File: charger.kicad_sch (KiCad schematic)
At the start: 14 parts, among them J5 USB_C_Receptacle_USB2.0_16P, Q1 BSS84, Q2 BSS670S2, U16 USBLC6-2SC6, U3 MIC5205-3.3YM5, U4 MCP73833-xxx-UN

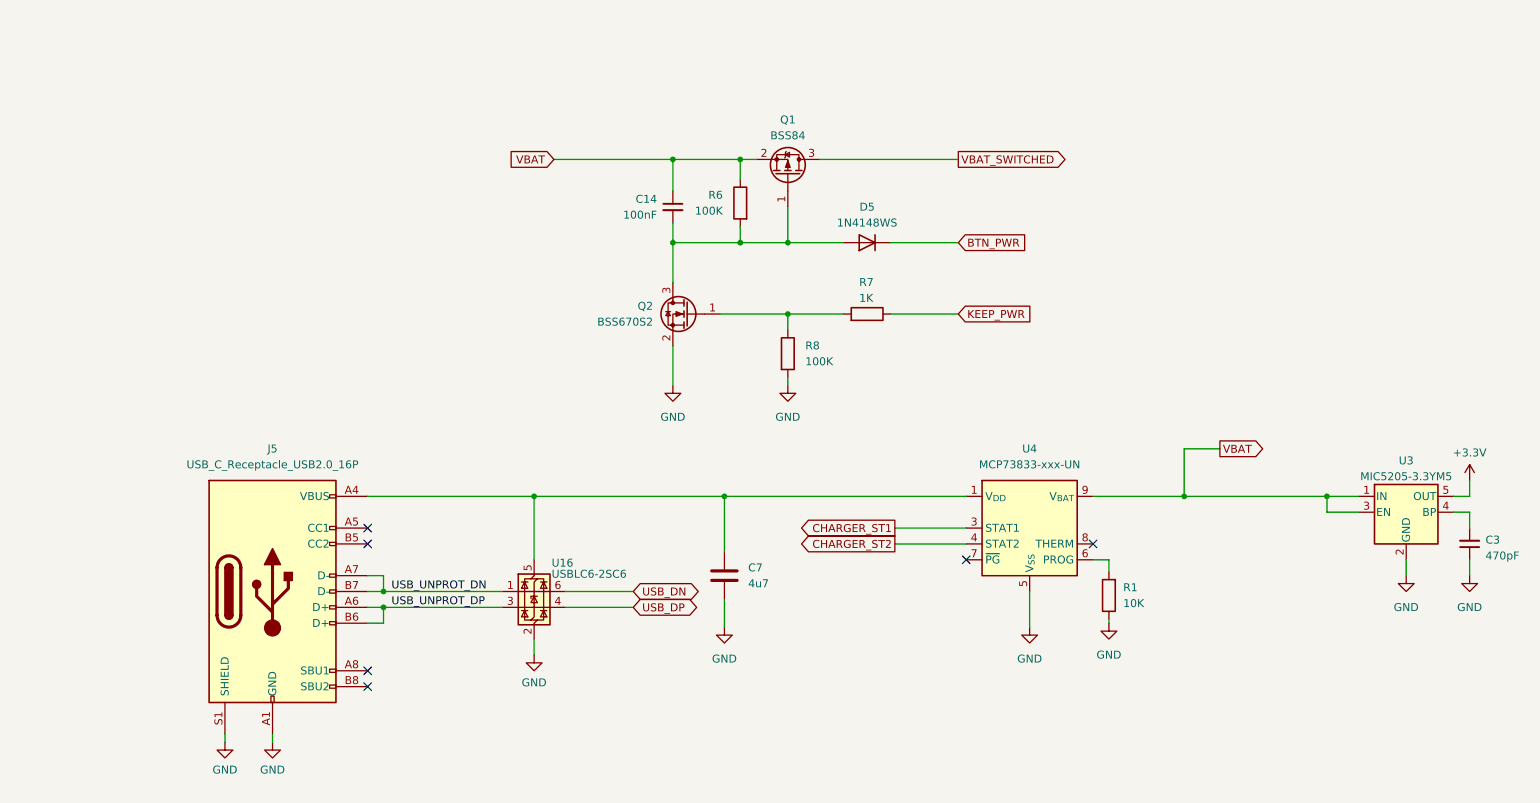
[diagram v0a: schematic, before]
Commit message: Board had been routedy
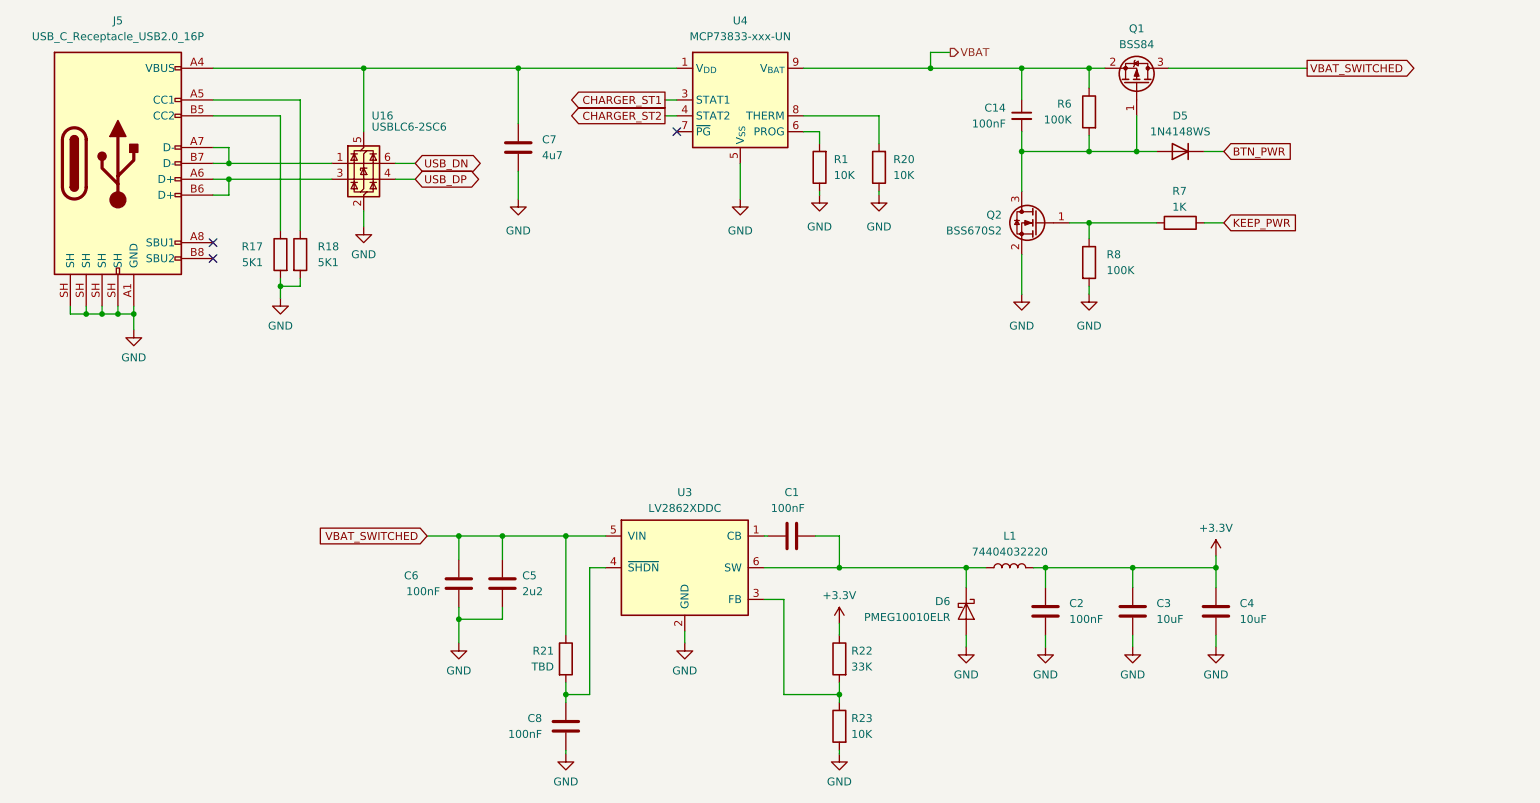
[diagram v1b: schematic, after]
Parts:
- removed C3: 470pF, Capacitor_SMD:C_0603_1608Metric, symbol Device:C_Small
- removed U3: MIC5205-3.3YM5, Package_TO_SOT_SMD:SOT-23-5, symbol Regulator_Linear:MIC5205-3.3YM5
- added C1, C2, C6, C8: 100nF, Capacitor_SMD:C_0603_1608Metric, symbol Device:C
- added C3: 10uF, Capacitor_SMD:C_0603_1608Metric, symbol Device:C
- added C4: 10uF, Capacitor_SMD:C_0805_2012Metric, symbol Device:C
- added C5: 2u2, Capacitor_SMD:C_0805_2012Metric, symbol Device:C
- added D6: PMEG10010ELR, Diode_SMD:Nexperia_CFP3_SOD-123W, symbol Diode:PMEG10010ELR
- added L1: 74404032220, Inductor_SMD:L_Wuerth_MAPI-3015, symbol Device:L
- added R17, R18: 5K1, Resistor_SMD:R_0603_1608Metric, symbol Device:R
- added R20, R23: 10K, Resistor_SMD:R_0603_1608Metric, symbol Device:R
- added R21: TBD, Resistor_SMD:R_0603_1608Metric, symbol Device:R
- added R22: 33K, Resistor_SMD:R_0603_1608Metric, symbol Device:R
- added U3: LV2862XDDC, Package_TO_SOT_SMD:SOT-23-6, symbol Regulator_Switching:LV2862XDDC
- R1: footprint Resistor_SMD:R_0402_1005Metric -> Resistor_SMD:R_0603_1608Metric
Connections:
- net +3.3V: now also C2.2, C3.2, C4.2, L1.2, R22.1
- net GND: now also J5.SH, C2.1, C3.1, C4.1, C5.1, C6.1, C8.1, D6.2 (A), R17.2, R18.2, R20.1, R23.2, U3.2 (GND); no longer J5.S1 (SHIELD)
- net VBAT_SWITCHED: now also C5.2, C6.2, R21.1, U3.5 (VIN)
- net at J5.A5 (CC1): now also R18.1
- net at J5.B5 (CC2): now also R17.1
- net at U4.8 (THERM): now also R20.2
- new net: C1.2, D6.1 (K), L1.1, U3.6 (SW)
- new net: C1.1, U3.1 (CB)
- new net: R22.2, R23.1, U3.3 (FB)
- new net: C8.2, R21.2, U3.4 (~{SHDN})
- no-connect marks 6 -> 3
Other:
- moved on the sheet: C14, C7, D5, Q1, Q2, R1, R6, R7, R8, U16, U4

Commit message: Daily save
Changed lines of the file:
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@@
 	(wire
 		(pts
-			(xy 94.615 106.045) (xy 99.695 106.045)
+			(xy 83.82 106.045) (xy 99.695 106.045)
 		)
 		(stroke
@@
 	(global_label "VBAT_SWITCHED"
 		(shape input)
-		(at 94.615 106.045 180)
+		(at 83.82 106.045 180)
 		(fields_autoplaced yes)
 		(effects
@@
 		)
 		(property "Intersheetrefs" "${INTERSHEET_REFS}"
-			(at 76.9946 106.045 0)
+			(at 66.1996 106.045 0)
 			(hide yes)
 			(show_name no)
@@
 		)
 	)
+	(group "charger"
+		(lib_id "martonmiklos:charger")
+		(members "01e84fd5-f747-4020-8fd6-b8dcc2b74338" "03a726e8-f3e8-403e-924a-5ef765c4f7fc"
+			"03f131bc-6628-429a-b0a5-e3f5afa171e4" "0b628756-8c00-452b-a3bd-ef999dcb8288"
+			"0b82a914-d713-4daf-9dc4-990cb81dc069" "15827e9a-85e8-4dd6-bc7d-e9f6ff24fd2d"
+			"15aa98e9-b72d-46e3-ab74-56cddecf5905" "173c6623-909e-4824-a967-7bd19a3c97d4"
+			"238347b0-2046-4f9f-bff6-a5b2ada0af1e" "247ee5cc-030c-499e-9d8b-42cf448516b7"
+			"2b1602a1-1bb2-4b2e-9c42-5471c2828bd8" "2b3f2cf4-1d8e-4fd8-8ea6-2a000066a748"
+			"2b5e59b9-4754-44b4-a9e3-1f4f43548eff" "376efd5a-dcb1-49ac-a426-d0f8d062c864"
+			"377687a4-20e1-429a-927b-2d6216137319" "3c8d662e-433a-4f96-8204-c6cd305cf2e5"
+			"3f5b5540-a644-4c20-b592-0d633b188111" "3fde2300-c87d-4f69-a114-242149a44162"
+			"41765163-874c-43af-afa4-44d000001fc7" "442cabfd-17f5-4520-9de1-67ccdf6128c3"
+			"4453b4e2-24bb-4e59-8092-f0588bce46a0" "488b77b0-993e-4126-9e9e-be032d7f7890"
+			"4947df85-bb2c-4b75-b2ea-5ab3492b03b4" "4990c6a4-f824-4d5c-8455-599c775c8ad1"
+			"4adec73d-67c0-4a8b-b247-3fe800ffe248" "4ed56fd3-6be7-4b9e-853e-a8b9b717d92c"
+			"50a1eb87-f90e-4274-8e3c-f7c2477b2a9d" "51d7c8de-3539-4ee9-9edc-b2976a9c465b"
+			"52450477-23f9-4c73-acf5-7c7c3b8b462e" "55b3fa5f-76c7-49db-8516-2348f296e36e"
+			"5655d3c4-d9a3-429c-92f8-097bd0b7afd1" "5a170b1c-98c5-4d4d-a57b-8be4ebf1ed0f"
+			"5cfed881-f50f-46e9-8914-ab80adff6d16" "613ccada-4610-40d0-8e92-0e1ed197e285"
+			"65766a60-7b75-44ee-a0a9-f5928501c4b7" "676ae03b-85a6-4a64-85ba-633ca9625658"
+			"6c652ae5-12ce-464d-8867-881209a80aeb" "76a2fdcf-4a87-499f-80a2-e44584066a7d"
+			"7904565b-1804-4336-889a-a4ce34178e21" "7eb14095-606c-4043-a32c-7274450ad052"
+			"82acc906-3b09-4950-8317-9efc5bac570c" "8715af0d-f789-451c-887d-52f29fb580c9"
+			"8aa6c538-0075-4573-b337-a18bd0b0a999" "8f2a7e35-5af3-447e-a823-93f6e491f942"
+			"91127fee-99b5-4e89-91a1-d7f753c85a87" "92a9fef8-3b15-4087-a0ad-d5eff69b5456"
+			"954f9562-1f7b-4ee5-839e-3407e6830d32" "9a4b5429-6889-4350-84d7-955d2c48a51b"
+			"9e49f6a7-135d-4d5b-bfb8-e23c5b1003ae" "9e6087be-e4e2-4034-85cd-a9c03fec03cc"
+			"9e69fab5-6437-419a-b22c-62ba6257170f" "a329b400-aeb3-44c2-894a-a76a0c8a55cc"
+			"a55610d4-96c6-4b30-b669-a3477d539bc6" "af45645e-0808-4134-aa6b-30d80b51711b"
+			"b4252efc-8d8f-42ec-9a0a-9338a0eb963f" "b930e5d8-374a-45dd-ae95-636f2f37bd8c"
+			"ba6ce36a-0c0c-4108-9d7d-7e64598c8630" "c07f3d91-b843-4dbd-99e1-fca94b3a66ca"
+			"c0a90cf4-4a55-4374-a9bf-3989e4863e6c" "c6b61dfb-ee0a-4562-a8b9-56d9b76ccede"
+			"c8e050ec-9292-455e-be54-59a5045505df" "cab6d48f-280d-4847-8fed-58624293725e"
+			"d01c1a5a-76bc-41bc-8fbc-b3b1f135eab2" "d32b1390-5b97-4bc7-be1b-0c3d5a2c7d6c"
+			"d5301903-7853-4a4f-b1d2-98e446f9da44" "d977d903-5b8d-4033-b940-bdd63cd45899"
+			"dacc7684-80b4-42e3-bdfa-cbfbd7d937d3" "dd3d8281-aa25-4eb4-b398-115e747f2429"
+			"dfbbc0ec-bccd-4ab5-9d07-a9031f097520" "e257e428-dfda-4b94-8c25-5496fb3572c7"
+			"eaa5426a-4688-4a86-be32-3b3d47176716" "eea9cf9b-3310-4f76-90d0-d70196977fb1"
+			"f40f9a2f-bff7-44f5-a3e5-c153ce8c3d83" "f4703d30-40ed-4269-af45-912fe57692e9"
+			"f4bb5658-0ca5-4871-a56c-a383a53557fa" "f506f3ed-d37d-4dd5-b521-7b0235e6fb8c"
+		)
+	)
